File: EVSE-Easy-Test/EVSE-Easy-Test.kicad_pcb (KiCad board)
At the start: 2 copper layers, 13 parts, among them J1 Type 2, J2 CP diag, SW1 PP current coding, SW2 CP state coding

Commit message: completed and sent to aisler
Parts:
- added REF**: MountingHole_3.2mm_M3_ISO7380_Pad, Mounting_Holes:MountingHole_3.2mm_M3_ISO7380_Pad, F.Cu at (106.7, 44.5)
- added REF**: MountingHole_3.2mm_M3_ISO7380_Pad, Mounting_Holes:MountingHole_3.2mm_M3_ISO7380_Pad, F.Cu at (44.5, 44.5)
- added REF**: MountingHole_3.2mm_M3_ISO7380_Pad, Mounting_Holes:MountingHole_3.2mm_M3_ISO7380_Pad, F.Cu at (44.5, 77.5)
- added REF**: MountingHole_3.2mm_M3_ISO7380_Pad, Mounting_Holes:MountingHole_3.2mm_M3_ISO7380_Pad, F.Cu at (106.7, 77.5)
- SW1: value PP current coding -> PP current
- SW2: value CP state coding -> CP state
- moved R8 15.2 mm to (59.1, 77.5), turned to 180 degrees
- moved J2 5.08 mm to (98.4, 77.5)
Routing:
- net CP: track 40.6 -> 38.0 mm
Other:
- board text added: "13"
- board text added: "20"
- board text added: "32"
- board text added: "63"
- board text added: "A"
- board text added: "B"
- board text added: "C"
- board text added: "CP"
- board text added: "D"
- board text added: "E"
- board text added: "EVSE Easy Test"
- board text added: "EVSE Easy Test v0.1 Mathias Dalheimer"
- board text added: "NC"
- board text added: "PE"
- board text added: "PP"
- board text added: "diode fault"
- board text added: "invalid"

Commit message: now with real edge cuts! now really ordered at aisler.net!
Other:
- board outline added: 70.1 x 40.9 mm
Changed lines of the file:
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@@
   (general
     (thickness 1.6)
-    (drawings 23)
+    (drawings 27)
     (tracks 47)
     (zones 0)
@@
     (pad 1 thru_hole circle (at 0 0) (size 5.7 5.7) (drill 3.2) (layers *.Cu *.Mask))
   )
+  (gr_line (start 40.513 40.513) (end 40.513 81.407) (layer Edge.Cuts) (width 0.15))
+  (gr_line (start 110.617 40.513) (end 40.513 40.513) (layer Edge.Cuts) (width 0.15))
+  (gr_line (start 110.617 81.407) (end 110.617 40.513) (layer Edge.Cuts) (width 0.15))
+  (gr_line (start 40.513 81.407) (end 110.617 81.407) (layer Edge.Cuts) (width 0.15))
   (gr_text "diode\nfault" (at 88.9 54.61) (layer F.SilkS)
     (effects (font (size 1 1) (thickness 0.25)))

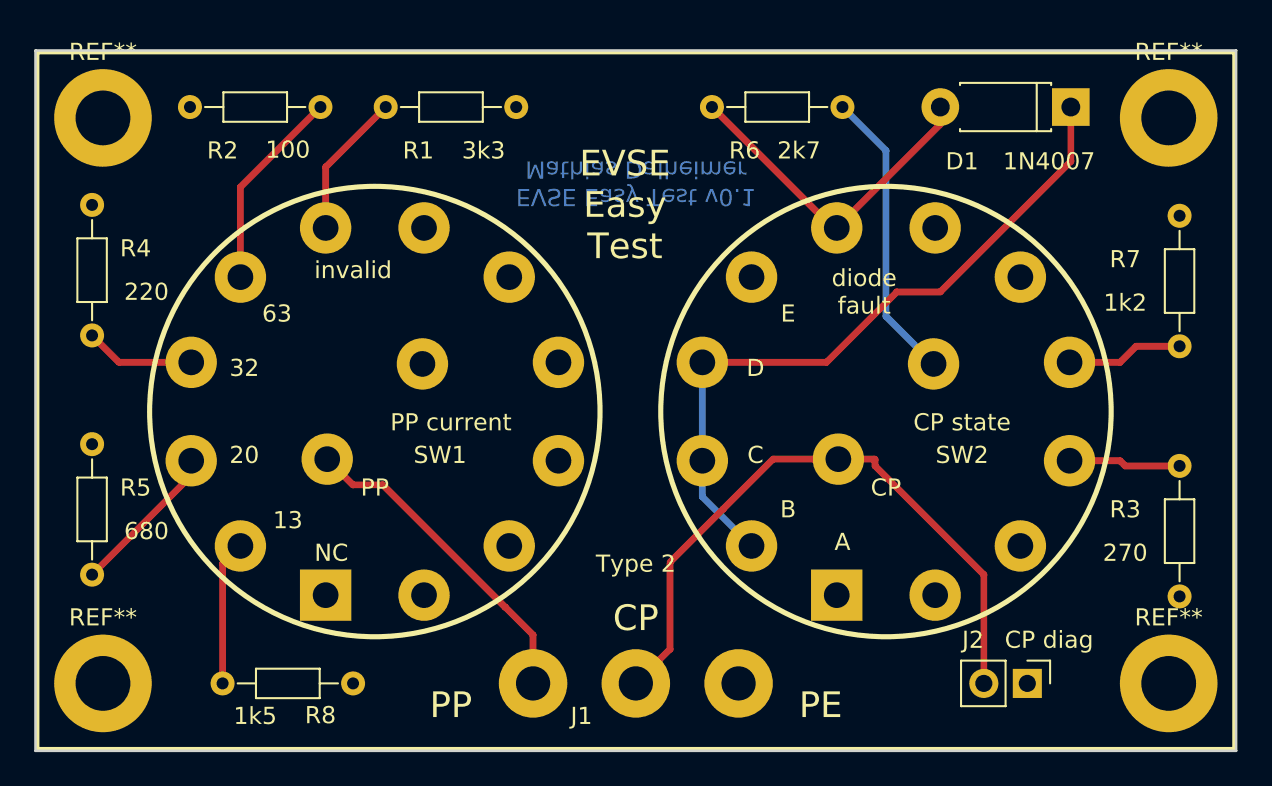
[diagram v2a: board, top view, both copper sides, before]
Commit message: final (?!?) changes to aisler.net order.
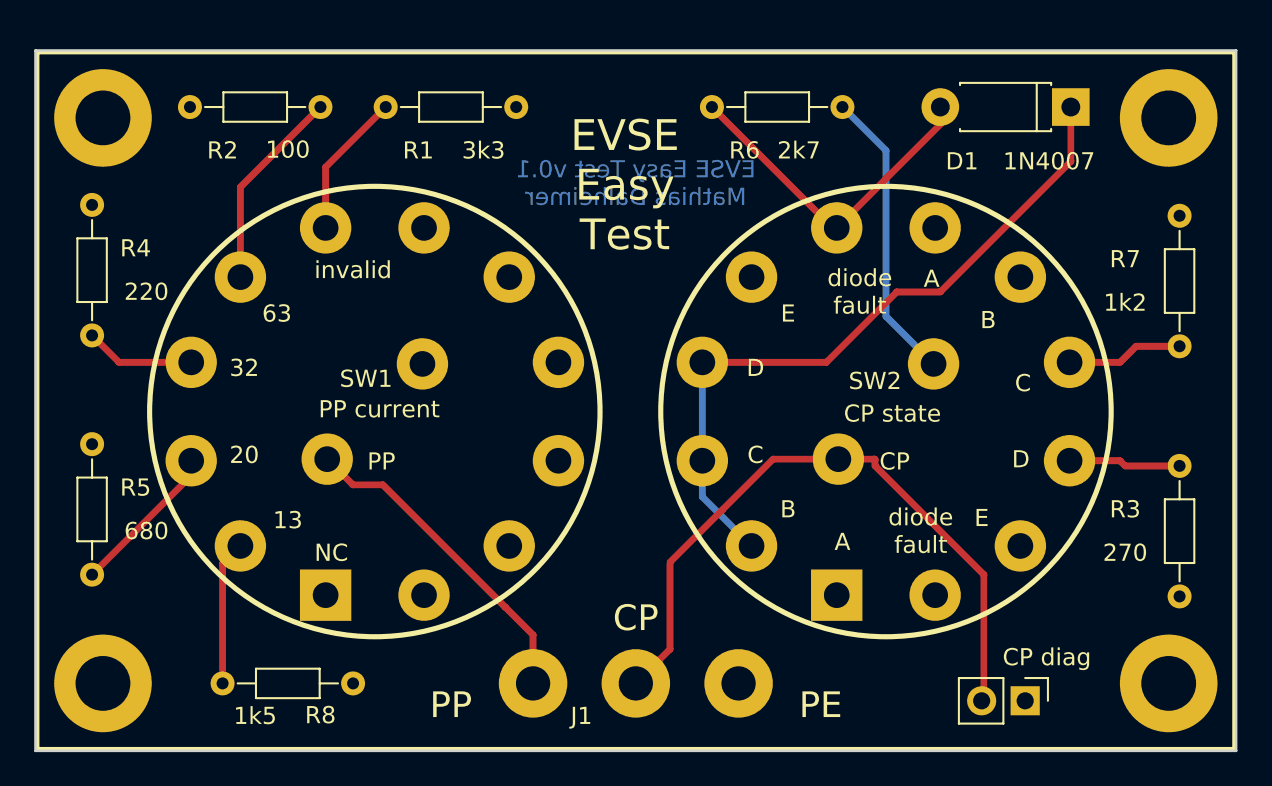
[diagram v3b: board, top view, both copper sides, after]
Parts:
- moved J2 1.02 mm to (98.3, 78.5)
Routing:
- net CP: track 38.0 -> 39.1 mm
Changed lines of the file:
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@@
   (general
     (thickness 1.6)
-    (drawings 27)
-    (tracks 47)
+    (drawings 33)
+    (tracks 48)
     (zones 0)
     (modules 17)
@@
       (effects (font (size 1 1) (thickness 0.15)))
     )
-    (fp_text value "Type 2" (at 0 6.985 180) (layer F.SilkS)
+    (fp_text value "Type 2" (at 0 6.985 180) (layer F.SilkS) hide
       (effects (font (size 1 1) (thickness 0.15)))
     )
@@
   )
   (module Pin_Headers:Pin_Header_Straight_1x02_Pitch2.54mm (layer F.Cu)
-    (at 98.425 77.47 270)
+    (at 98.298 78.486 270)
     (descr "Through hole straight pin header, 1x02, 2.54mm pitch, single row")
     (tags "Through hole pin header THT 1x02 2.54mm single row")
-    (fp_text reference J2 (at -2.54 3.175) (layer F.SilkS)
+    (fp_text reference J2 (at -2.54 3.175) (layer F.SilkS) hide
       (effects (font (size 1 1) (thickness 0.15)))
     )
@@
   (module local:LorlinCK-1060 (layer F.Cu)
     (at 60.325 61.595)
-    (fp_text reference SW1 (at 3.81 2.54) (layer F.SilkS)
-      (effects (font (size 1 1) (thickness 0.15)))
-    )
-    (fp_text value "PP current" (at 4.445 0.635) (layer F.SilkS)
+    (fp_text reference SW1 (at -0.508 -1.905) (layer F.SilkS)
+      (effects (font (size 1 1) (thickness 0.15)))
+    )
+    (fp_text value "PP current" (at 0.254 -0.127) (layer F.SilkS)
       (effects (font (size 1 1) (thickness 0.15)))
     )
@@
   (module local:LorlinCK-1060 (layer F.Cu)
     (at 90.17 61.595)
-    (fp_text reference SW2 (at 4.445 2.54) (layer F.SilkS)
-      (effects (font (size 1 1) (thickness 0.15)))
-    )
-    (fp_text value "CP state" (at 4.445 0.635) (layer F.SilkS)
+    (fp_text reference SW2 (at -0.635 -1.778) (layer F.SilkS)
+      (effects (font (size 1 1) (thickness 0.15)))
+    )
+    (fp_text value "CP state" (at 0.381 0.127) (layer F.SilkS)
       (effects (font (size 1 1) (thickness 0.15)))
     )
@@
     (tags "mounting hole 3.2mm m3 iso7380")
     (attr virtual)
-    (fp_text reference REF** (at 0 -3.85) (layer F.SilkS)
+    (fp_text reference REF** (at 0 -3.85) (layer F.SilkS) hide
       (effects (font (size 1 1) (thickness 0.15)))
     )
@@
     (tags "mounting hole 3.2mm m3 iso7380")
     (attr virtual)
-    (fp_text reference REF** (at 0 -3.85) (layer F.SilkS)
+    (fp_text reference REF** (at 0 -3.85) (layer F.SilkS) hide
       (effects (font (size 1 1) (thickness 0.15)))
     )
@@
     (tags "mounting hole 3.2mm m3 iso7380")
     (attr virtual)
-    (fp_text reference REF** (at 0 -3.85) (layer F.SilkS)
+    (fp_text reference REF** (at 0 -3.85) (layer F.SilkS) hide
       (effects (font (size 1 1) (thickness 0.15)))
     )
@@
     (tags "mounting hole 3.2mm m3 iso7380")
     (attr virtual)
-    (fp_text reference REF** (at 0 -3.85) (layer F.SilkS)
+    (fp_text reference REF** (at 0 -3.85) (layer F.SilkS) hide
       (effects (font (size 1 1) (thickness 0.15)))
     )
@@
     (fp_circle (center 0 0) (end 3.1 0) (layer F.CrtYd) (width 0.05))
     (pad 1 thru_hole circle (at 0 0) (size 5.7 5.7) (drill 3.2) (layers *.Cu *.Mask))
+  )
+  (gr_text "diode\nfault" (at 92.202 68.58) (layer F.SilkS)
+    (effects (font (size 1 1) (thickness 0.25)))
+  )
+  (gr_text E (at 95.758 67.818) (layer F.SilkS)
+    (effects (font (size 1 1) (thickness 0.25)))
+  )
+  (gr_text D (at 98.044 64.389) (layer F.SilkS)
+    (effects (font (size 1 1) (thickness 0.25)))
+  )
+  (gr_text C (at 98.171 59.944) (layer F.SilkS)
+    (effects (font (size 1 1) (thickness 0.25)))
+  )
+  (gr_text B (at 96.139 56.261) (layer F.SilkS)
+    (effects (font (size 1 1) (thickness 0.25)))
+  )
+  (gr_text A (at 92.837 53.848) (layer F.SilkS)
+    (effects (font (size 1 1) (thickness 0.25)))
   )
   (gr_line (start 40.513 40.513) (end 40.513 81.407) (layer Edge.Cuts) (width 0.15))
@@
   (gr_line (start 110.617 81.407) (end 110.617 40.513) (layer Edge.Cuts) (width 0.15))
   (gr_line (start 40.513 81.407) (end 110.617 81.407) (layer Edge.Cuts) (width 0.15))
-  (gr_text "diode\nfault" (at 88.9 54.61) (layer F.SilkS)
+  (gr_text "diode\nfault" (at 88.646 54.61) (layer F.SilkS)
     (effects (font (size 1 1) (thickness 0.25)))
   )
@@
     (effects (font (size 1 1) (thickness 0.25)))
   )
-  (gr_text CP (at 90.17 66.04) (layer F.SilkS)
+  (gr_text CP (at 90.678 64.516) (layer F.SilkS)
     (effects (font (size 1 1) (thickness 0.25)))
   )
@@
     (effects (font (size 1 1) (thickness 0.25)))
   )
-  (gr_text PP (at 60.325 66.04) (layer F.SilkS)
+  (gr_text PP (at 60.706 64.516) (layer F.SilkS)
     (effects (font (size 1 1) (thickness 0.25)))
   )
@@
     (effects (font (size 1.5 1.5) (thickness 0.3)))
   )
-  (gr_text "EVSE Easy Test v0.1\nMathias Dalheimer" (at 75.565 48.26 180) (layer B.Cu)
+  (gr_text "EVSE Easy Test v0.1\nMathias Dalheimer" (at 75.565 48.26) (layer B.Cu)
     (effects (font (size 1 1) (thickness 0.25)) (justify mirror))
   )
-  (gr_text "EVSE\nEasy\nTest" (at 74.93 49.53) (layer F.SilkS)
-    (effects (font (size 1.5 1.5) (thickness 0.3)))
+  (gr_text "EVSE\nEasy\nTest" (at 74.93 48.387) (layer F.SilkS)
+    (effects (font (size 1.8 1.8) (thickness 0.3)))
   )
   (gr_line (start 40.64 40.64) (end 110.49 40.64) (layer F.SilkS) (width 0.2))
@@
   (segment (start 80.645 67.31) (end 77.564999 70.390001) (width 0.4) (layer F.Cu) (net 4))
   (segment (start 77.564999 75.470001) (end 77.564999 70.485) (width 0.4) (layer F.Cu) (net 4))
-  (segment (start 89.51132 64.375) (end 87.39 64.375) (width 0.4) (layer F.Cu) (net 4))
-  (segment (start 95.885 77.47) (end 95.885 71.12) (width 0.4) (layer F.Cu) (net 4))
-  (segment (start 95.885 71.12) (end 89.535 64.77) (width 0.4) (layer F.Cu) (net 4))
-  (segment (start 89.535 64.77) (end 89.535 64.39868) (width 0.4) (layer F.Cu) (net 4))
-  (segment (start 89.535 64.39868) (end 89.51132 64.375) (width 0.4) (layer F.Cu) (net 4))
+  (segment (start 95.885 71.12) (end 95.885 78.359) (width 0.4) (layer F.Cu) (net 4))
+  (segment (start 87.39 64.375) (end 89.51132 64.375) (width 0.4) (layer F.Cu) (net 4))
+  (segment (start 89.51132 64.375) (end 89.535 64.39868) (width 0.4) (layer F.Cu) (net 4))
+  (segment (start 95.885 78.359) (end 95.758 78.486) (width 0.4) (layer F.Cu) (net 4))
+  (segment (start 89.535 64.39868) (end 89.535 64.77) (width 0.4) (layer F.Cu) (net 4))
+  (segment (start 89.535 64.77) (end 95.885 71.12) (width 0.4) (layer F.Cu) (net 4))
   (segment (start 57.452109 47.322891) (end 57.452109 50.873224) (width 0.4) (layer F.Cu) (net 6))
   (segment (start 60.96 43.815) (end 57.452109 47.322891) (width 0.4) (layer F.Cu) (net 6))

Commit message: second prototype as ordered
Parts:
- removed the REF** at (106.7, 44.5)
- removed the REF** at (44.5, 44.5)
- removed the REF** at (44.5, 77.5)
- removed the REF** at (106.7, 77.5)
- added REF**: MountingHole_3.2mm_M3, Mounting_Holes:MountingHole_3.2mm_M3, F.Cu at (107.2, 44.2)
- added REF**: MountingHole_3.2mm_M3, Mounting_Holes:MountingHole_3.2mm_M3, F.Cu at (43.8, 78.0)
- added REF**: MountingHole_3.2mm_M3, Mounting_Holes:MountingHole_3.2mm_M3, F.Cu at (43.8, 43.9)
- added REF**: MountingHole_3.2mm_M3, Mounting_Holes:MountingHole_3.2mm_M3, F.Cu at (106.9, 77.9)
- D1: footprint Diodes_THT:D_DO-41_SOD81_P7.62mm_Horizontal -> local:D_DO-41_SOD81_P7.62mm_Horizontal
- J1: footprint local:Type2-Solderpads -> local:RIACon175_3poles_AKL175-03; moved to B.Cu
- J2: footprint Pin_Headers:Pin_Header_Straight_1x02_Pitch2.54mm -> local:Pin_Header_Straight_1x02_Pitch2.54mm
- R1, R2, R3, R4, R5, R6, R7, R8: footprint Resistors_THT:R_Axial_DIN0204_L3.6mm_D1.6mm_P7.62mm_Horizontal -> local:R_Axial_DIN0204_L3.6mm_D1.6mm_P7.62mm_Horizontal
- moved R7 36.6 mm to (83.9, 78.4), turned to 0 degrees
- moved R4 36.0 mm to (79.8, 47.5), turned to 180 degrees
- moved J2 34.6 mm to (99.6, 43.9), turned to 90 degrees
- moved R5 19.5 mm to (56.5, 78.4), turned to 180 degrees
- moved R6 15.4 mm to (72.3, 43.8), turned to 0 degrees
- moved R3 13.9 mm to (94.7, 78.4), turned to 0 degrees
- moved R8 10.3 mm to (69.3, 78.2)
- moved D1 8.26 mm to (92.7, 43.8)
- moved J1 8.12 mm to (75.4, 69.3), turned to 90 degrees
- moved R2 6.61 mm to (56.1, 43.9), turned to 180 degrees
- moved SW2 4.33 mm to (94.5, 61.7)
- moved SW1 4.09 mm to (56.2, 61.4)
- moved R1 1.02 mm to (67.6, 43.9)
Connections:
- R6 pad 1: Net-(R6-Pad1) -> PE
- SW2 pad 1: (no net) -> Net-(D1-Pad2)
- SW2 pad 10: Net-(R3-Pad2) -> Net-(R7-Pad2)
- SW2 pad 11: (no net) -> Net-(R3-Pad2)
- SW2 pad 12: PE -> (no net)
- SW2 pad 14: Net-(R6-Pad1) -> Net-(D1-Pad2)
- SW2 pad 2: Net-(D1-Pad1) -> (no net)
- SW2 pad 5: PE -> Net-(D1-Pad1)
- SW2 pad 6: Net-(D1-Pad2) -> PE
- SW2 pad 7: (no net) -> Net-(R7-Pad2)
- SW2 pad 8: PE -> (no net)
- SW2 pad 9: Net-(R7-Pad2) -> (no net)
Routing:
- net Net-(R7-Pad2): track 6.81 -> 39.4 mm
- net Net-(R4-Pad2): track 6.44 -> 31.2 mm
- net Net-(D1-Pad2): track 19.8 -> 42.1 mm
- net Net-(R6-Pad1): track 17.2 -> 0.00 mm
- net Net-(D1-Pad1): track 41.5 -> 25.6 mm
- net PE: track 0.00 -> 15.4 mm, vias 0 -> 19
- net Net-(R8-Pad2): track 8.46 -> 18.3 mm
- net Net-(R5-Pad2): track 9.05 -> 15.8 mm
- net CP: track 39.1 -> 44.4 mm
- net PP: track 19.1 -> 22.9 mm
- net Net-(R2-Pad2): track 11.9 -> 9.61 mm
- net Net-(R3-Pad2): track 6.55 -> 8.78 mm
- net Net-(R1-Pad2): track 8.51 -> 9.41 mm
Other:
- board text added: "df"
